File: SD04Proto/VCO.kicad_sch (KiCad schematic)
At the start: 21 parts, among them IC1 74AHC04PW,118, IC2 74AHC1G4212GWH, IC3 74AHC2G08DP,125

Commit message: Small schematic changes
Moved R13, added some alternative parts
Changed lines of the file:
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@@
 	(symbol
 		(lib_id "SamacSys_Parts:74AHC04PW,118")
-		(at 200.66 107.95 0)
+		(at 199.39 127 0)
 		(unit 4)
 		(exclude_from_sim no)
@@
 		(fields_autoplaced yes)
 		(property "Reference" "IC1"
-			(at 228.6 101.6 0)
+			(at 227.33 120.65 0)
 			(show_name yes)
 			(effects
@@
 		)
 		(property "Value" "74AHC04PW,118"
-			(at 228.6 104.14 0)
+			(at 227.33 123.19 0)
 			(effects
 				(font
@@
 		)
 		(property "Footprint" "SOP65P640X110-14N"
-			(at 222.25 202.87 0)
+			(at 220.98 221.92 0)
 			(effects
 				(font
@@
 		)
 		(property "Datasheet" "https://assets.nexperia.com/documents/data-sheet/74AHC_AHCT04.pdf"
-			(at 222.25 302.87 0)
+			(at 220.98 321.92 0)
 			(effects
 				(font
@@
 		)
 		(property "Description" "74AHC(T)04 - hex inverter@en-us"
-			(at 200.66 107.95 0)
+			(at 199.39 127 0)
 			(effects
 				(font
@@
 		)
 		(property "Height" "1.1"
-			(at 222.25 502.87 0)
+			(at 220.98 521.92 0)
 			(effects
 				(font
@@
 		)
 		(property "Manufacturer_Name" "Nexperia"
-			(at 222.25 602.87 0)
+			(at 220.98 621.92 0)
 			(effects
 				(font
@@
 		)
 		(property "Manufacturer_Part_Number" "74AHC04PW,118"
-			(at 222.25 702.87 0)
+			(at 220.98 721.92 0)
 			(effects
 				(font
@@
 		)
 		(property "Mouser Part Number" "771-AHC04PW118"
-			(at 222.25 802.87 0)
+			(at 220.98 821.92 0)
 			(effects
 				(font
@@
 		)
 		(property "Mouser Price/Stock" "https://www.mouser.co.uk/ProductDetail/Nexperia/74AHC04PW118?qs=P62ublwmbi%2FFq01vg0%252B6Ww%3D%3D"
-			(at 222.25 902.87 0)
+			(at 220.98 921.92 0)
 			(effects
 				(font
@@
 		)
 		(property "Arrow Part Number" "74AHC04PW,118"
-			(at 222.25 1002.87 0)
+			(at 220.98 1021.92 0)
 			(effects
 				(font
@@
 		)
 		(property "Arrow Price/Stock" "https://www.arrow.com/en/products/74ahc04pw118/nexperia?region=nac"
-			(at 222.25 1102.87 0)
+			(at 220.98 1121.92 0)
 			(effects
 				(font
@@
 		)
 		(property "Nedap Part Number" ""
-			(at 200.66 107.95 0)
+			(at 199.39 127 0)
 			(effects
 				(font

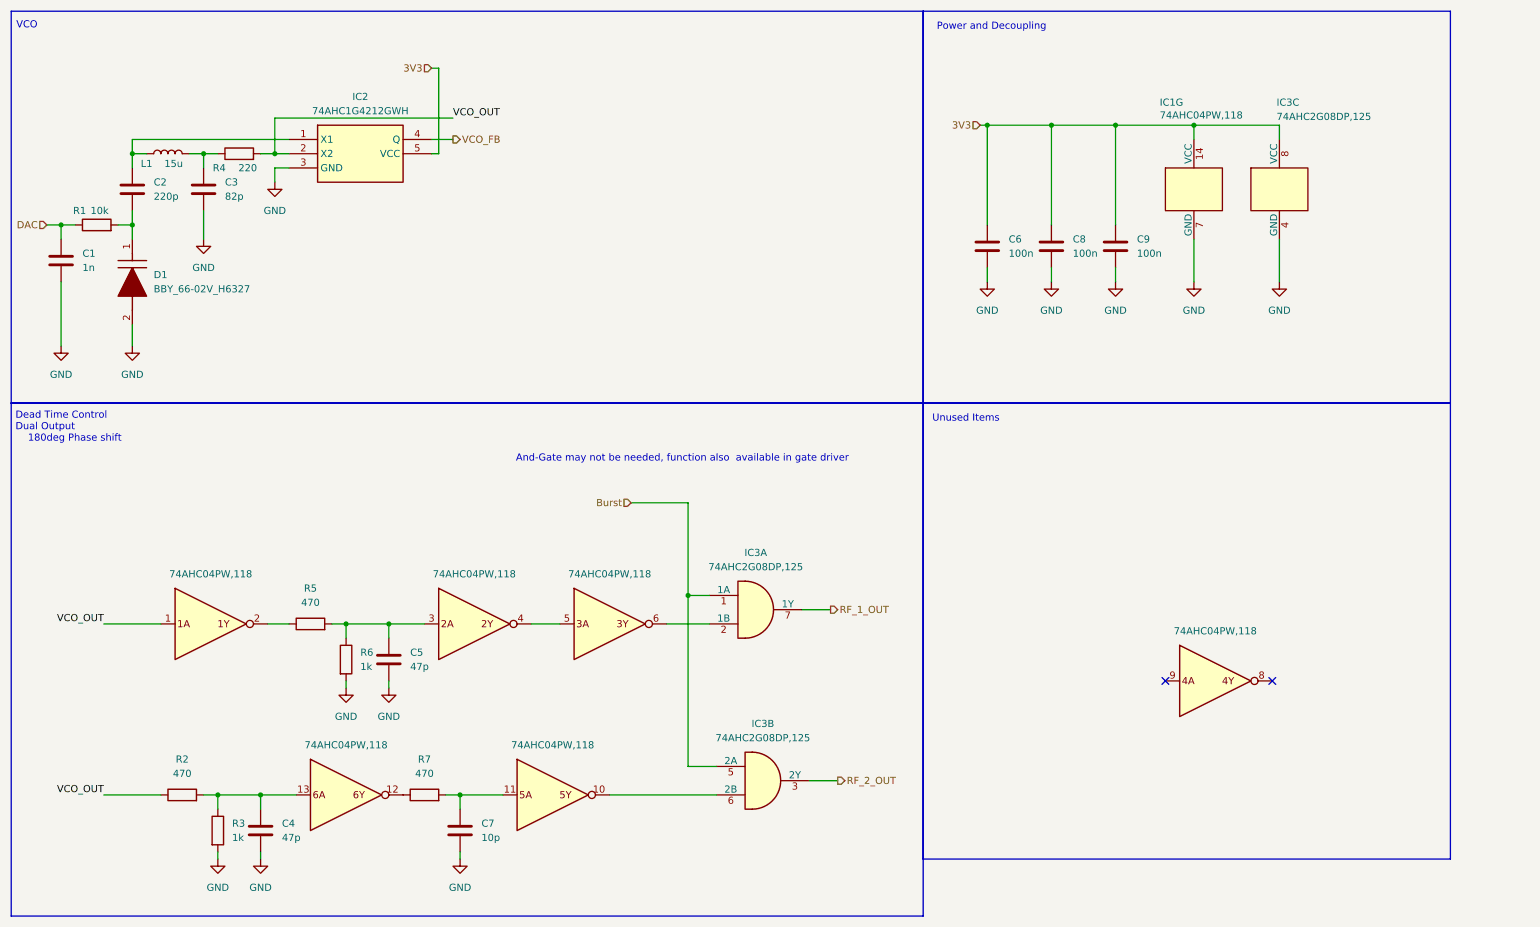
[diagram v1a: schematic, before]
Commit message: Added PLL
Added PLL, power supplies started, Microcontroller Started
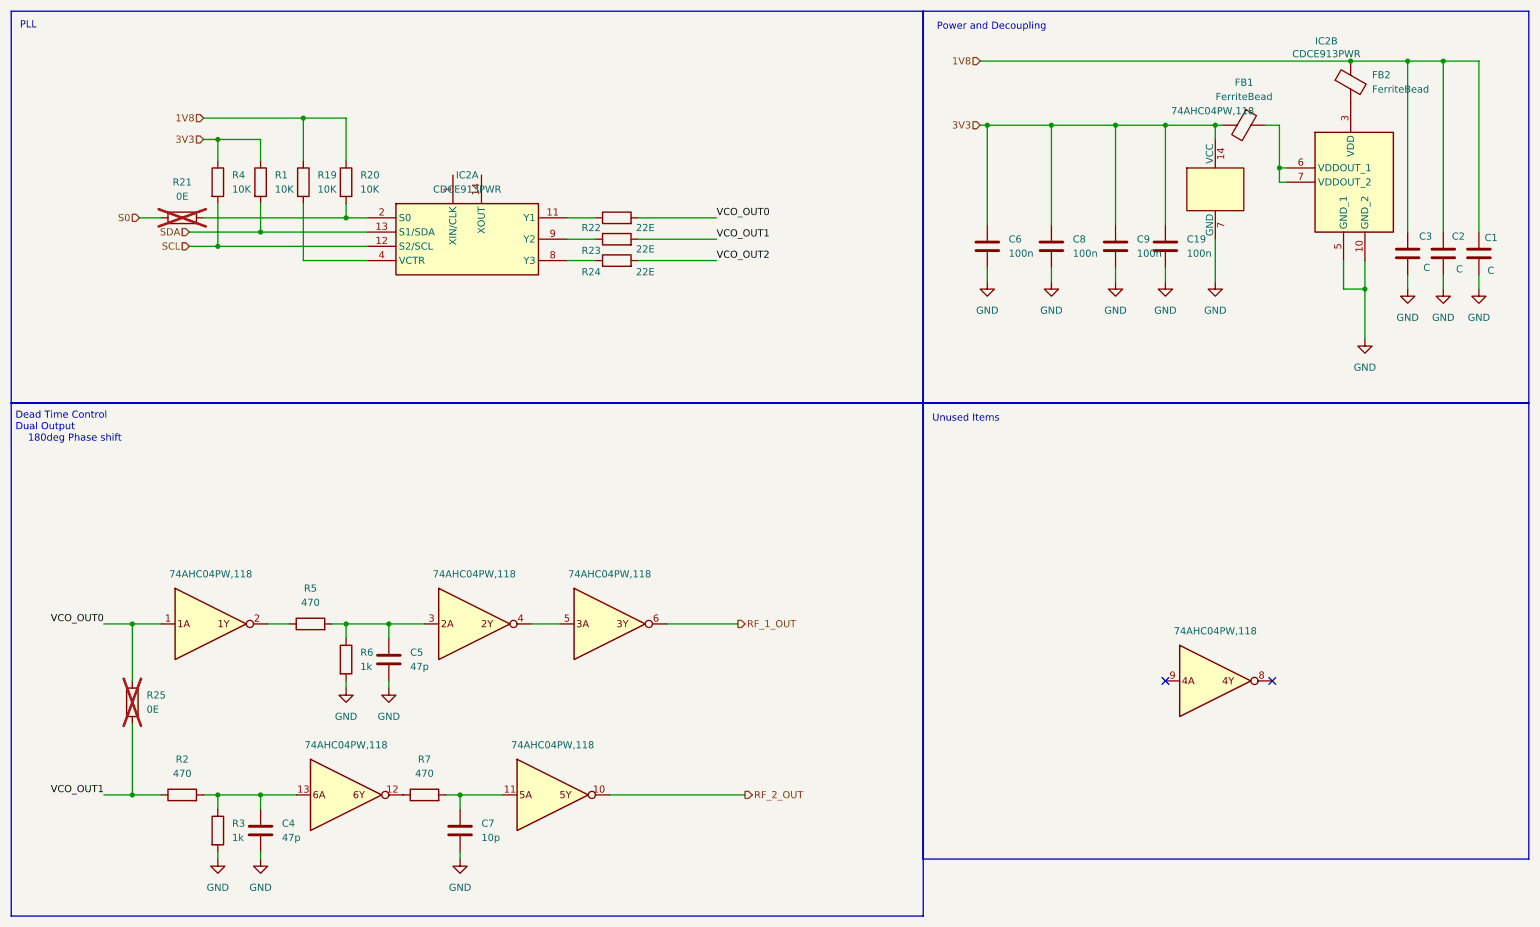
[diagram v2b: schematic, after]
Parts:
- removed D1: BBY_66-02V_H6327, SODFL1608X59N, symbol SamacSys_Parts:BBY_66-02V_H6327
- removed unit 7 of IC1
- removed IC2: 74AHC1G4212GWH, SOT65P212X110-5N, symbol SamacSys_Parts:74AHC1G4212GWH
- removed IC3: 74AHC2G08DP,125, SOP65P400X110-8N, symbol SamacSys_Parts:74AHC2G08DP,125
- removed L1: 15u, Inductor_SMD:L_1210_3225Metric, symbol Device:L
- added C19: 100n, symbol Device:C
- added FB1, FB2: FerriteBead, symbol Device:FerriteBead
- added IC2: CDCE913PWR, SOP65P640X120-14N, symbol SamacSys_Parts:CDCE913PWR
- added R19, R20: 10K, symbol Device:R
- added R21, R25: 0E, symbol Device:R
- added R22, R23, R24: 22E, symbol Device:R
- C1: value 1n -> C; footprint Capacitor_SMD:C_0603_1608Metric -> (none)
- C2: value 220p -> C; footprint Capacitor_SMD:C_0603_1608Metric -> (none)
- C3: value 82p -> C
- C6: Placement IC2 VCC decoupling -> IC2 VCC decoupling 1
- C9: Placement IC3 VCC decoupling -> IC2 VCC decoupling 2
- R1: value 10k -> 10K
- R4: value 220 -> 10K
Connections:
- net 3V3: now also IC1.14 (VCC), R1.1, R4.1, C19.1, FB1.2
- net GND: now also C2.2, IC1.7 (GND), C19.2, IC2.10 (GND_2), IC2.5 (GND_1)
- net RF_1_OUT: now also IC1.6
- net RF_2_OUT: now also IC1.10
- net 1V8: now reaches C2.1
- net 1V8: now also C1.1, C3.1, FB2.1, R19.1, R20.1
- net SDA: now reaches R1.2
- net SDA: now also IC2.13 (S1/SDA); no longer C2.2
- removed net DAC: C1.1, R1.1
- removed net VCO_OUT: IC1.1, R2.1, R4.2
- new net: IC2.8 (Y3), R24.1
- new net: IC2.9 (Y2), R23.1
- new net: IC2.2 (S0), R20.2, R21.2
- new net: FB2.2, IC2.3 (VDD)
- new net: FB1.1, IC2.6 (VDDOUT_1), IC2.7 (VDDOUT_2)
- new net: IC2.11 (Y1), R22.1
- new net: IC2.4 (VCTR), R19.2
- new net S0: R21.1
- new net SCL: IC2.12 (S2/SCL), R4.2
- new net VCO_OUT0: IC1.1, R22.2, R25.1
- new net VCO_OUT1: R2.1, R23.2, R25.2
- new net VCO_OUT2: R24.2
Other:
- note added: "PLL"
- note removed: "And-Gate may not be needed, function also available in gate driver"
- note removed: "VCO"

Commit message: added enable switch and load, boostconverter
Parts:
- added unit 5 of IC1
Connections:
- net RF_2_OUT: now also IC1.10; no longer IC1.10
- net at C7.2, R7.2: now also IC1.11; no longer IC1.11
